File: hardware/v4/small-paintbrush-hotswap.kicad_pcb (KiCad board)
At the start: 2 copper layers, 94 x 47 mm, 17 parts, among them J1 Conn_01x02, J2 Conn_01x04, J3 Conn_01x04, SW1 SW_SPDT, SW2 SW_SPDT, U1 ProMicro, U2 ProMicro

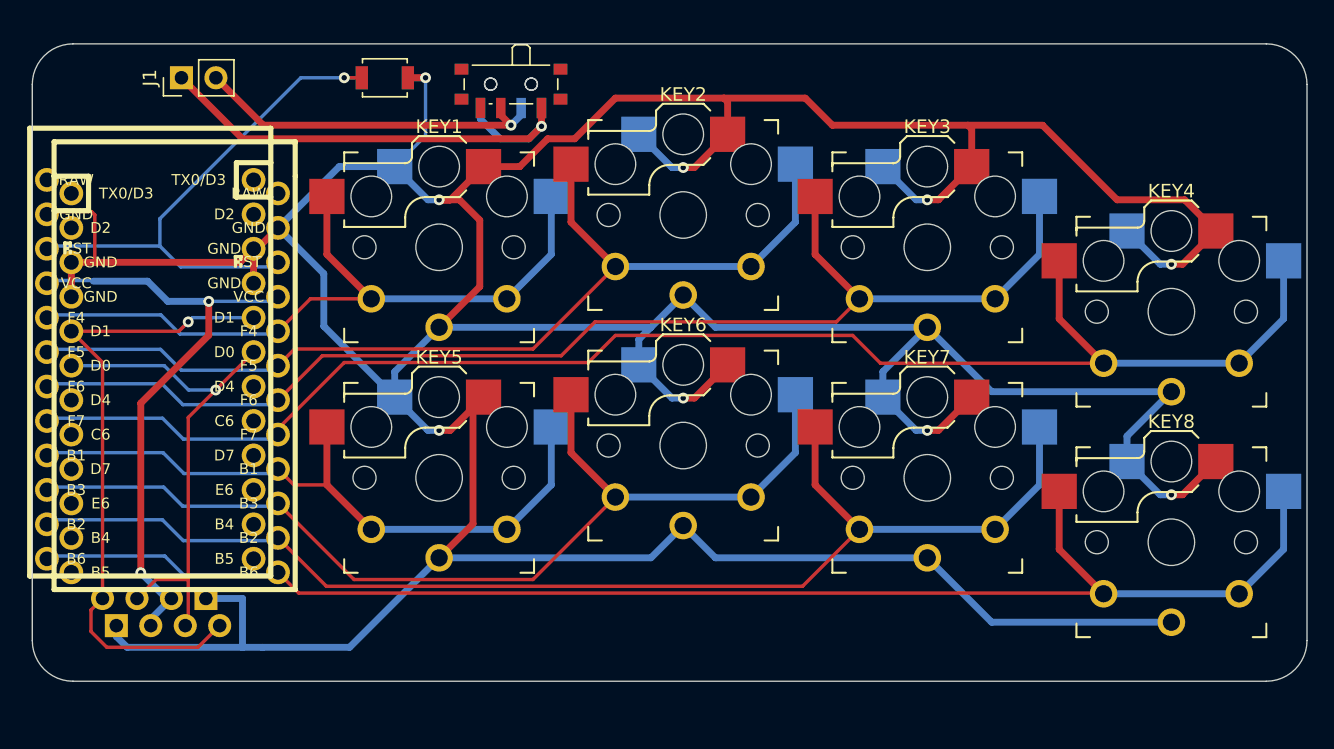
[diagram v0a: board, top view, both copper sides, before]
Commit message: Rev v4 to add tap holes
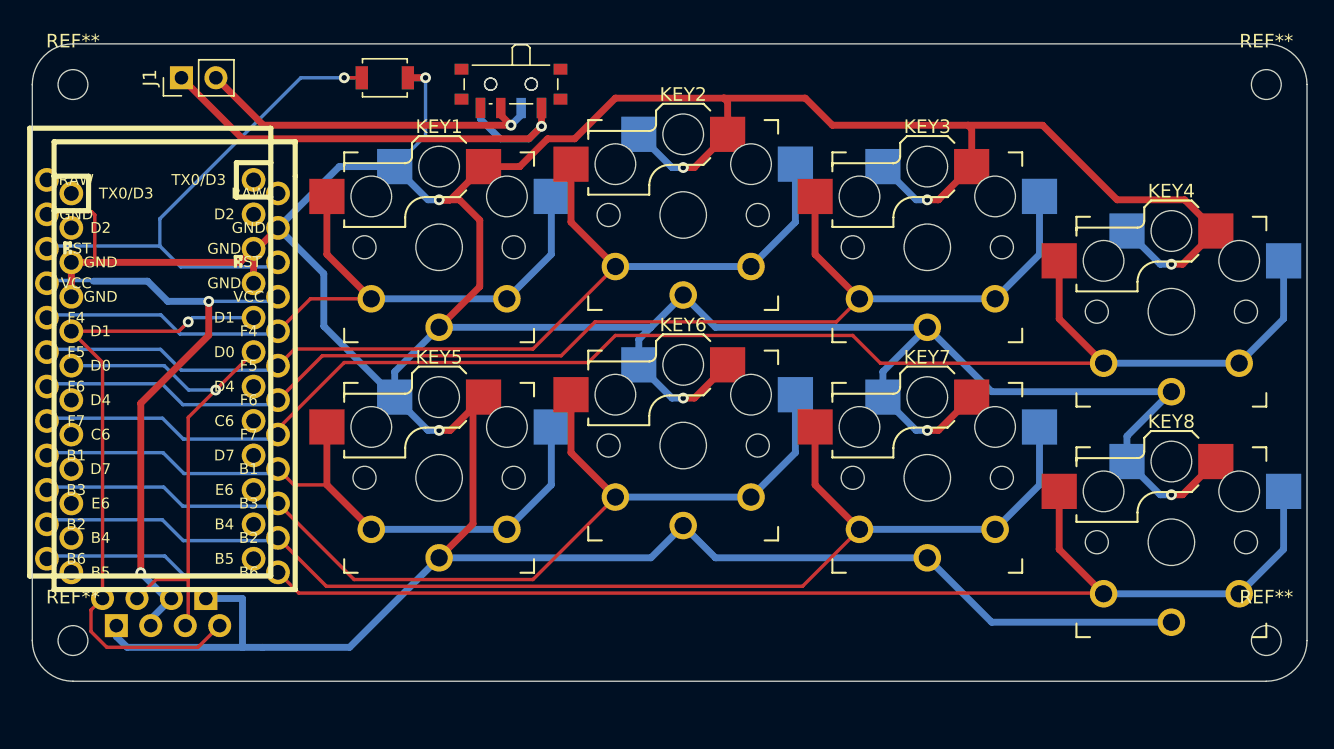
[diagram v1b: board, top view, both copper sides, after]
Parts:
- added REF**: MountingHole_2.2mm_M2, MountingHole:MountingHole_2.2mm_M2, F.Cu at (78.9, 62.6)
- added REF**: MountingHole_2.2mm_M2, MountingHole:MountingHole_2.2mm_M2, F.Cu at (78.9, 21.6)
- added REF**: MountingHole_2.2mm_M2, MountingHole:MountingHole_2.2mm_M2, F.Cu at (166.9, 21.6)
- added REF**: MountingHole_2.2mm_M2, MountingHole:MountingHole_2.2mm_M2, F.Cu at (166.9, 62.6)

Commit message: Update v4 hardware to include stand off holes and move the reset button / power switch to better locations
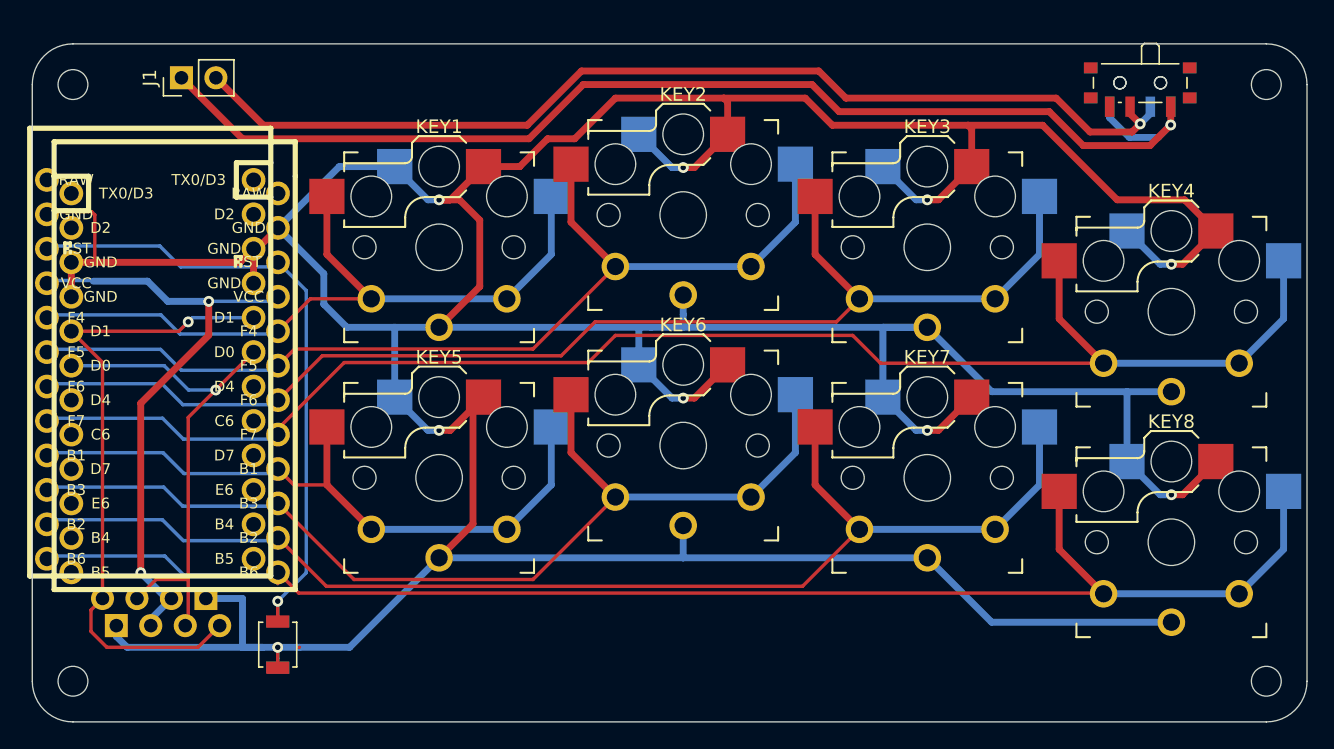
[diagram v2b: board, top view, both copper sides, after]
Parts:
- moved SW1 46.4 mm to (157.6, 21.8)
- moved SW2 46.4 mm to (157.6, 21.8)
- moved PUSH1 42.5 mm to (94.0, 62.9), turned to 270 degrees
- moved PUSH2 42.5 mm to (94.0, 62.9), turned to 270 degrees
- moved REF** 3.00 mm to (78.9, 65.6)
- moved REF** 3.00 mm to (166.9, 65.6)
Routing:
- net Net-(J1-Pad1): track 36.4 -> 86.6 mm
- net Net-(J1-Pad2): track 26.4 -> 76.5 mm
- net RST: track 40.4 -> 47.6 mm
- net GND: track 399.3 -> 393.5 mm
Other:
- board size 94 x 47 mm -> 94 x 50 mm
